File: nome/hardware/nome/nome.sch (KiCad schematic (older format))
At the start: 51 parts, among them J1 Audio-Jack-3_2Switches, J2 Conn_02x05_Odd_Even, J3 Barrel_Jack, J4 Conn_01x04, SW1 SW_SPST, SW2 Rotary_Encoder_Switch, U1 LM1117-1.8, U2 LM1117-3.3, U3 AS1115, U4 STMF411CEU6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

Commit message: Add LTC footprint
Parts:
- U5: footprint Displays_7-Segment:LTC-4727JS -> nome:LTC-4727
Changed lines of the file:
@@
 F 0 "U5" H 6200 8600 50  0000 C CNN
 F 1 "LTC-4727JS" H 7920 8600 50  0000 C CNN
-F 2 "Displays_7-Segment:LTC-4727JS" H 7150 7550 50  0001 C CNN
+F 2 "nome:LTC-4727" H 7150 7550 50  0001 C CNN
 F 3 "" H 6770 8180 50  0001 C CNN
 	1    7150 8150

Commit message: Add PEC11 footprint
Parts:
- SW2: footprint (none) -> nome:PEC11
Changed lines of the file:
@@
 F 0 "SW2" H 2200 9910 50  0000 C CNN
 F 1 "Rotary_Encoder_Switch" H 2200 9390 50  0000 C CNN
-F 2 "" H 2100 9810 50  0001 C CNN
+F 2 "nome:PEC11" H 2100 9810 50  0001 C CNN
 F 3 "" H 2200 9910 50  0001 C CNN
 	1    2200 9650

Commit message: Add switch footprint
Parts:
- removed SW1: SW_SPST, symbol SW_SPST
- added SW1: SW_SPDT, symbol SW_SPDT
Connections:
- no-connect marks 39 -> 40

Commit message: Add speaker wire pads
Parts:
- LS1: footprint (none) -> nome:WirePad-1x2-2.54mm
- SW1: footprint (none) -> nome:CK_SPDT

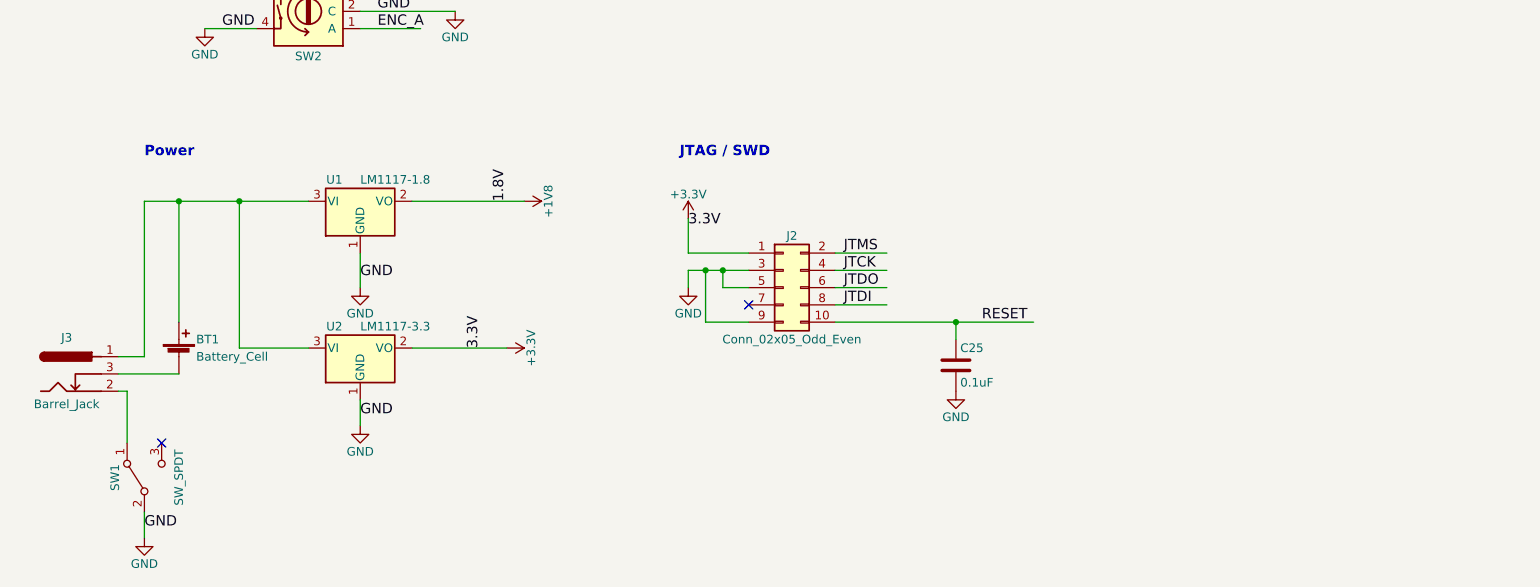
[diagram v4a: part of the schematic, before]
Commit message: Add in Lipo charger circuit, with USB
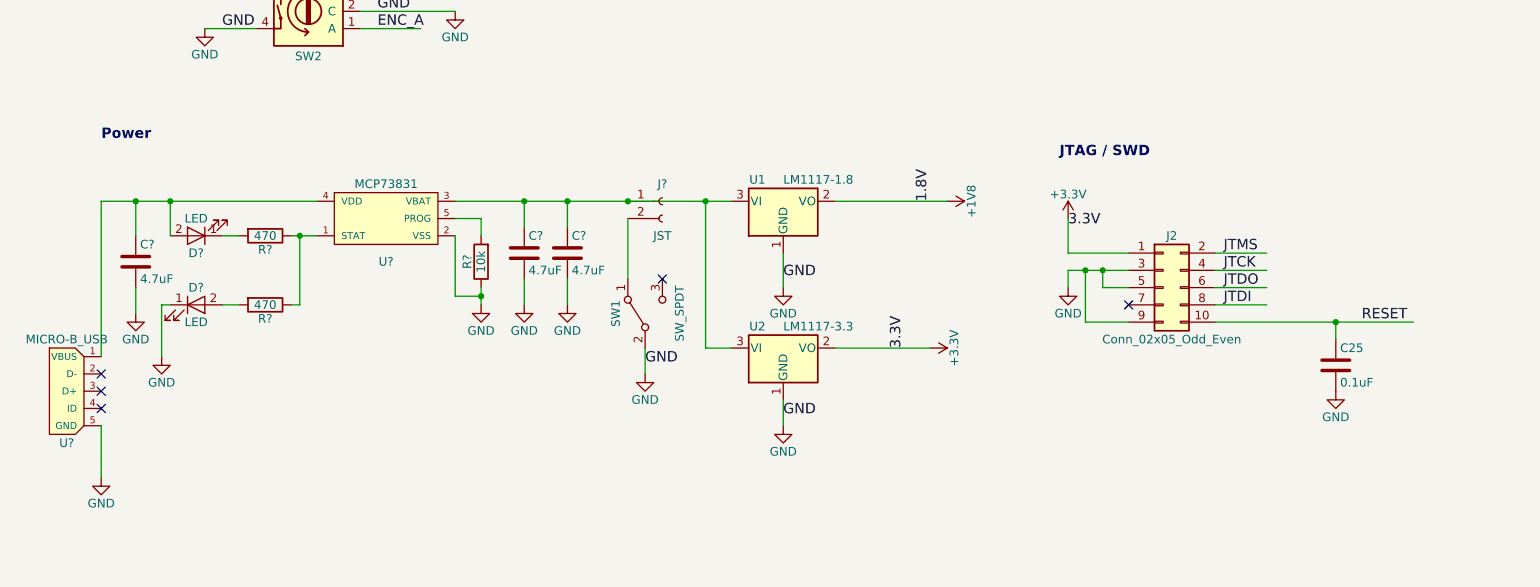
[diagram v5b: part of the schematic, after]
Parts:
- removed BT1: Battery_Cell, symbol Battery_Cell
- removed J3: Barrel_Jack, symbol Barrel_Jack
- added C? (x3): 4.7uF, symbol C
- added D? (x2): LED, symbol LED
- added J?: JST, symbol Conn_01x02_Female
- added R?: 10k, symbol R
- added R? (x2): 470, symbol R
- added U?: MCP73831, symbol MCP73831
- added U?: MICRO-B_USB, symbol MICRO-B_USB
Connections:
- wire segments 229 -> 246
- no-connect marks 40 -> 43
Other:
- moved on the sheet: C25, J2, SW1, U1, U2

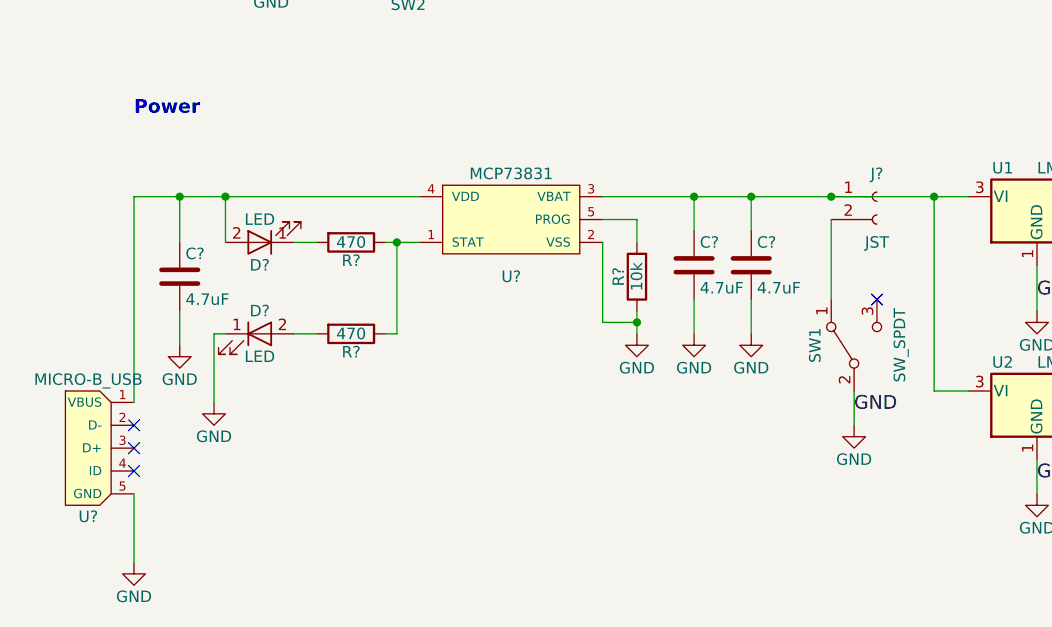
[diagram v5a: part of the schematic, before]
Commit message: Annotate missing components
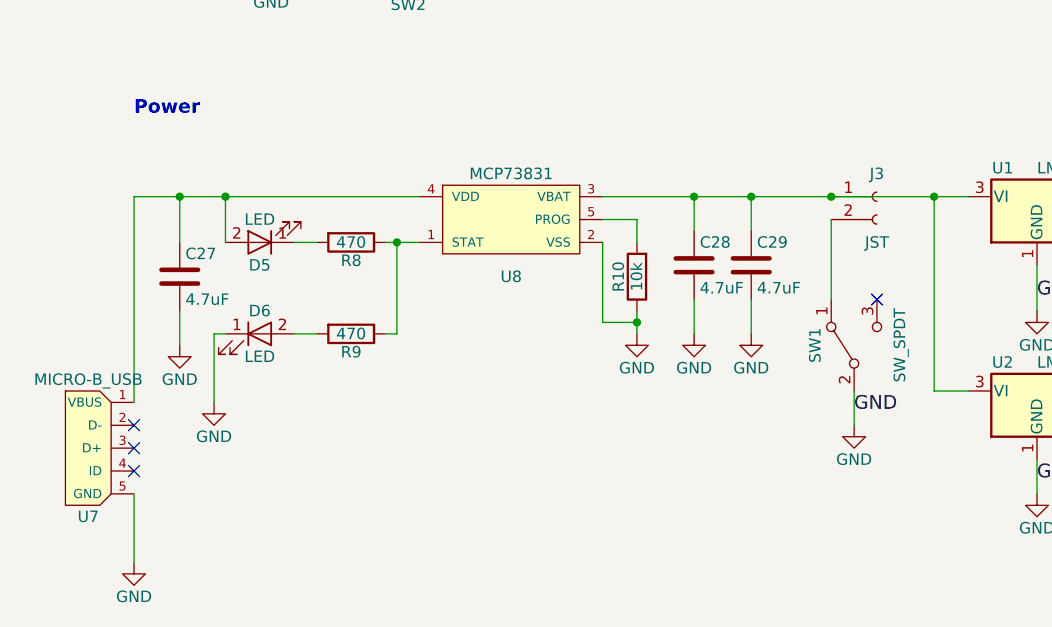
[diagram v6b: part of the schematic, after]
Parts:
- gave numbers to parts that had none: 11

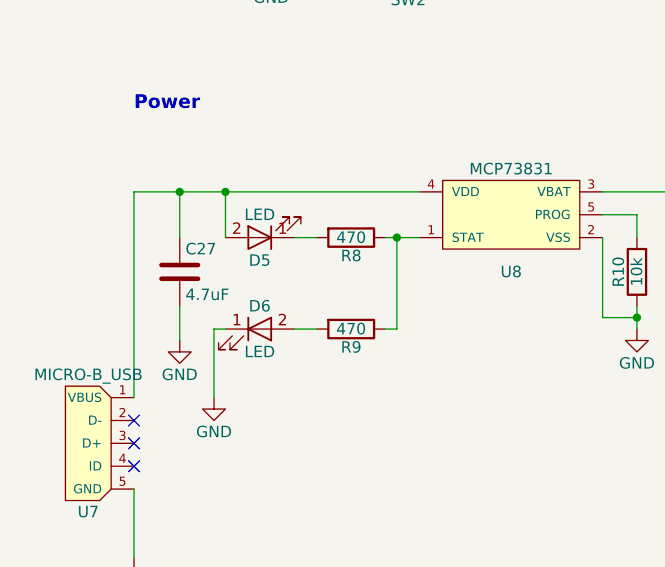
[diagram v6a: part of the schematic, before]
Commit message: Add JST connector
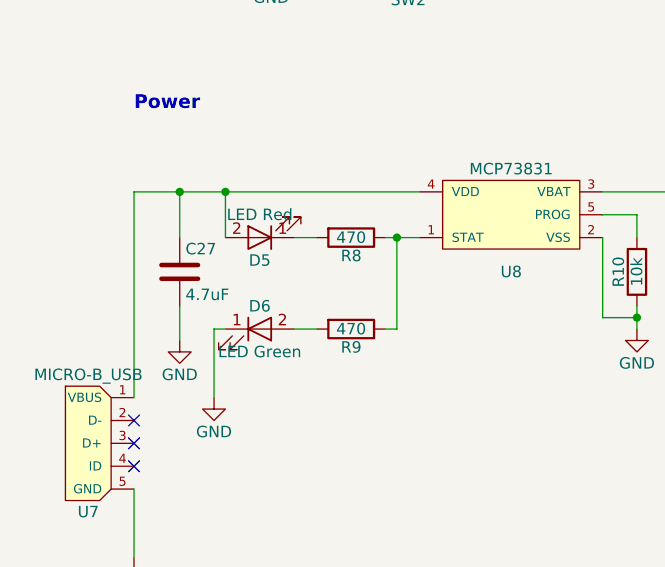
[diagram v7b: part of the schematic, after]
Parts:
- C27, C28, C29: footprint (none) -> Capacitors_SMD:C_0805_HandSoldering
- D5: value LED -> LED Red; footprint (none) -> LEDs:LED_0805_HandSoldering
- D6: value LED -> LED Green; footprint (none) -> LEDs:LED_0805_HandSoldering
- J3: footprint (none) -> third_party:JST_PH_B2B-PH-SM4-TB_02x2.00mm_Straight
- R10, R8, R9: footprint (none) -> Resistors_SMD:R_0805_HandSoldering
- U7: footprint (none) -> open-project:MICRO-B_USB
- U8: footprint (none) -> TO_SOT_Packages_SMD:SOT-23-5_HandSoldering

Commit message: Finish up footprints
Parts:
- J1: footprint (none) -> nome:SJ-2524
- J2: value Conn_02x05_Odd_Even -> JTAG_SWD
- J4: value Conn_01x04 -> 7SEG_DEBUG
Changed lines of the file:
@@
 F 0 "J1" H 14200 2390 50  0000 C CNN
 F 1 "Audio-Jack-3_2Switches" H 13500 1850 50  0000 L CNN
-F 2 "" H 14450 2200 50  0001 C CNN
+F 2 "nome:SJ-2524" H 14450 2200 50  0001 C CNN
 F 3 "" H 14450 2200 50  0001 C CNN
 	1    14200 2100
@@
 P 7150 11250
 F 0 "J2" H 7200 11550 50  0000 C CNN
-F 1 "Conn_02x05_Odd_Even" H 7200 10950 50  0000 C CNN
+F 1 "JTAG_SWD" H 7200 10950 50  0000 C CNN
 F 2 "Pin_Headers:Pin_Header_Straight_2x10_Pitch2.54mm" H 7150 11250 50  0001 C CNN
 F 3 "" H 7150 11250 50  0001 C CNN
@@
 P 1700 7400
 F 0 "J4" H 1700 7600 50  0000 C CNN
-F 1 "Conn_01x04" H 1700 7100 50  0000 C CNN
+F 1 "7SEG_DEBUG" H 1700 7100 50  0000 C CNN
 F 2 "Pin_Headers:Pin_Header_Straight_1x04_Pitch2.54mm" H 1700 7400 50  0001 C CNN
 F 3 "" H 1700 7400 50  0001 C CNN
